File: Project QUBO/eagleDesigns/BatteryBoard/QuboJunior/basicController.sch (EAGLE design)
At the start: 11 parts, among them IC1 74AHCT1G08DBV, Q1 FDN5618P

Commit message: Final Design
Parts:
- added BATT, T_FUSE, WATER: (no value), pinhead:PINHD-1X2
- added C2, C6: 10nF, resistor:C-USC0805
- added C3, C5, C7: 100nF, resistor:C-USC0805
- added C4, C8: T491D475K050AT, resistor:CPOL-USCT7343
- added D1, D2: MMSD4148, diode:DIODE-SOD123
- added IC2: TLC2272D, texas:TLC2272D
- added IC3: 74LVC1G08DBV, 74xx-little-us:74LVC1G08DBV
- added LED1: Green, led:LEDCHIP-LED0805
- added R10, R4: 115k, resistor:R-US_R0805
- added R11, R6, R9: 1M, resistor:R-US_R0805
- added R12, R15, R17, R18: 100k, resistor:R-US_R0805
- added R13, R14, R5: 10k, resistor:R-US_R0805
- added R16: 470, resistor:R-US_R0805
- added R19: (no value), resistor:R-TRIMM3314J
- added R3: 845k, resistor:R-US_R0805
- added R7, R8: 3.3k, resistor:R-US_R0805
- added SK_DISABLE, SK_DISABLE1, TH_DISABLE: (no value), jumper:JP1E
- added U1, U2: LT3063, linear:LT3063
- IC1: value 74AHCT1G08DBV -> 74LVC1G08DBV; device 74xx-little-us:74AHCT1G08DBV -> 74xx-little-us:74LVC1G08DBV
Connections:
- removed net V+: Q1.D, R1.2
- new net BATT: BATT.1, Q1.D, R1.2
- new net N$10: IC2B.-IN, R12.2, R14.1
- new net N$11: IC2B.+IN, R17.1, R18.2
- new net N$12: R16.2, WATER.1
- new net N$13: R14.2, R15.2, R16.1
- new net N$14: IC2A.OUT, SK_DISABLE1.1
- new net N$15: IC2A.+IN, R19.S
- new net N$6: C2.1, U1.REF/BYP
- new net N$7: C6.1, U2.REF/BYP
- new net N$8: IC1A.I1, R11.2, TH_DISABLE.1, T_FUSE.2
- new net N$9: IC2A.-IN, IC2B.OUT, R12.1
- new net ON_SW: D1.C, ON.3, ON.4, ON_SW.1
- new net RELAY: C7.1, R9.2, U2.OUT
- new net SK: C5.1, IC3A.I0, R5.1, R6.2, SK_DISABLE.1
- new net SOFT_KILL: R5.2
- new net WATER: IC1A.I0, SK_DISABLE1.2
- net +5V: now also C3.1, IC2P.VCC, IC3P.VCC, R15.1, R17.2, R19.A, R3.2, SK_DISABLE.2, TH_DISABLE.2, T_FUSE.1, U1.OUT; no longer IC1P.VCC
- net FAULT: now also IC1A.O, IC3A.I1, OFF.3, OFF.4, OFF_SW.1; no longer IC1A.I0
- net FET: now also IC3A.O, R13.2; no longer IC1A.O
- net GND: now also BATT.2, C2.2, C3.2, C4.-, C5.2, C6.2, C7.2, C8.-, D2.A, IC2P.GND, IC3P.GND, LED1.C, ON.1, ON.2, ON_SW.2, R10.1, R11.1, R13.1, R18.1, R19.E, R4.1, R6.1, RELAY.2, U1.GND, U2.GND, WATER.2; no longer IC1P.GND
- net N$1: now also R10.2, R9.1, U2.ADJ; no longer ON.1, ON.2, ON_SW.2
- net N$2: now also R3.1, R4.2, U1.ADJ; no longer ON.3, ON.4, ON_SW.1
- net N$4: now also D1.A
- net N$5: now also LED1.A, R7.1, R8.1; no longer IC1A.I1, OFF.3, OFF.4, OFF_SW.1
- net VDD: now also C4.+, C8.+, D2.C, R7.2, R8.2, RELAY.1, U1.IN, U1.SHDN, U2.IN, U2.SHDN
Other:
- note added: "10V LDO"
- note added: "5V LDO"
- note added: "Connectors"
- note added: "Main Gate Control"
- note added: "Off Switch"
- note added: "On Indicator"
- note added: "On Switch"
- note added: "Power Switching"
- note added: "Secondary AND Gate"
- note added: "Water Sensor Amplifier"
- moved on the sheet: C1, IC1, N1, OFF, OFF_SW, ON, ON_SW, Q1, R1, R2, RELAY

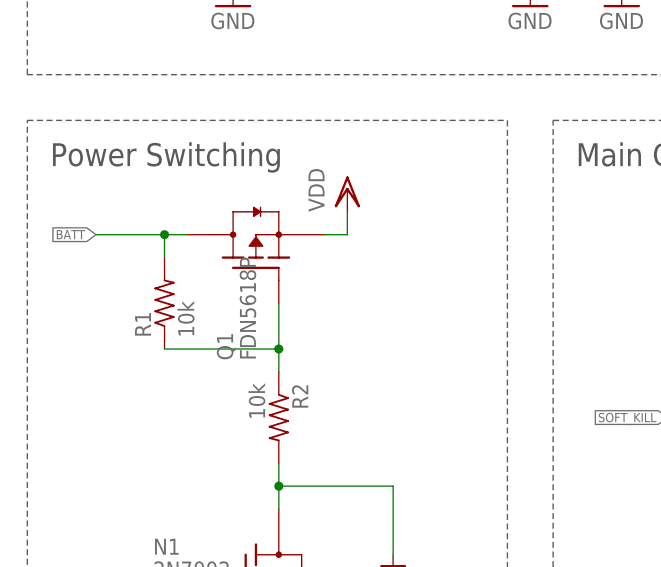
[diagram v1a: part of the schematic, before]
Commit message: 
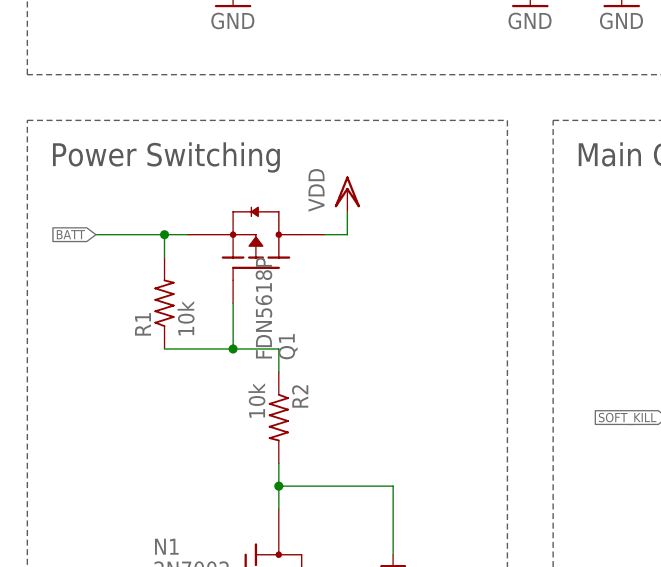
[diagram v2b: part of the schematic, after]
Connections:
- net BATT: now also Q1.S; no longer Q1.D
- net VDD: now also Q1.D; no longer Q1.S
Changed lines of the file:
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@@
 <?xml version="1.0" encoding="utf-8"?>
 <!DOCTYPE eagle SYSTEM "eagle.dtd">
-<eagle version="6.5.0">
+<eagle version="8.1.0">
 <drawing>
 <settings>
@@
 <grid distance="0.1" unitdist="inch" unit="inch" style="lines" multiple="1" display="no" altdistance="0.01" altunitdist="inch" altunit="inch"/>
 <layers>
-<layer number="1" name="Top" color="4" fill="1" visible="yes" active="no"/>
-<layer number="2" name="Route2" color="1" fill="3" visible="yes" active="no"/>
-<layer number="3" name="Route3" color="4" fill="3" visible="yes" active="no"/>
-<layer number="4" name="Route4" color="1" fill="4" visible="yes" active="no"/>
-<layer number="5" name="Route5" color="4" fill="4" visible="yes" active="no"/>
-<layer number="6" name="Route6" color="1" fill="8" visible="yes" active="no"/>
-<layer number="7" name="Route7" color="4" fill="8" visible="yes" active="no"/>
-<layer number="8" name="Route8" color="1" fill="2" visible="yes" active="no"/>
-<layer number="9" name="Route9" color="4" fill="2" visible="yes" active="no"/>
-<layer number="10" name="Route10" color="1" fill="7" visible="yes" active="no"/>
-<layer number="11" name="Route11" color="4" fill="7" visible="yes" active="no"/>
-<layer number="12" name="Route12" color="1" fill="5" visible="yes" active="no"/>
-<layer number="13" name="Route13" color="4" fill="5" visible="yes" active="no"/>
-<layer number="14" name="Route14" color="1" fill="6" visible="yes" active="no"/>
-<layer number="15" name="Route15" color="4" fill="6" visible="yes" active="no"/>
-<layer number="16" name="Bottom" color="1" fill="1" visible="yes" active="no"/>
-<layer number="17" name="Pads" color="2" fill="1" visible="yes" active="no"/>
-<layer number="18" name="Vias" color="2" fill="1" visible="yes" active="no"/>
-<layer number="19" name="Unrouted" color="6" fill="1" visible="yes" active="no"/>
-<layer number="20" name="Dimension" color="15" fill="1" visible="yes" active="no"/>
-<layer number="21" name="tPlace" color="7" fill="1" visible="yes" active="no"/>
-<layer number="22" name="bPlace" color="7" fill="1" visible="yes" active="no"/>
-<layer number="23" name="tOrigins" color="15" fill="1" visible="yes" active="no"/>
-<layer number="24" name="bOrigins" color="15" fill="1" visible="yes" active="no"/>
-<layer number="25" name="tNames" color="7" fill="1" visible="yes" active="no"/>
-<layer number="26" name="bNames" color="7" fill="1" visible="yes" active="no"/>
-<layer number="27" name="tValues" color="7" fill="1" visible="yes" active="no"/>
-<layer number="28" name="bValues" color="7" fill="1" visible="yes" active="no"/>
+<layer number="1" name="Top" color="4" fill="1" visible="no" active="no"/>
+<layer number="2" name="Route2" color="1" fill="3" visible="no" active="no"/>
+<layer number="3" name="Route3" color="4" fill="3" visible="no" active="no"/>
+<layer number="4" name="Route4" color="1" fill="4" visible="no" active="no"/>
+<layer number="5" name="Route5" color="4" fill="4" visible="no" active="no"/>
+<layer number="6" name="Route6" color="1" fill="8" visible="no" active="no"/>
+<layer number="7" name="Route7" color="4" fill="8" visible="no" active="no"/>
+<layer number="8" name="Route8" color="1" fill="2" visible="no" active="no"/>
+<layer number="9" name="Route9" color="4" fill="2" visible="no" active="no"/>
+<layer number="10" name="Route10" color="1" fill="7" visible="no" active="no"/>
+<layer number="11" name="Route11" color="4" fill="7" visible="no" active="no"/>
+<layer number="12" name="Route12" color="1" fill="5" visible="no" active="no"/>
+<layer number="13" name="Route13" color="4" fill="5" visible="no" active="no"/>
+<layer number="14" name="Route14" color="1" fill="6" visible="no" active="no"/>
+<layer number="15" name="Route15" color="4" fill="6" visible="no" active="no"/>
+<layer number="16" name="Bottom" color="1" fill="1" visible="no" active="no"/>
+<layer number="17" name="Pads" color="2" fill="1" visible="no" active="no"/>
+<layer number="18" name="Vias" color="2" fill="1" visible="no" active="no"/>
+<layer number="19" name="Unrouted" color="6" fill="1" visible="no" active="no"/>
+<layer number="20" name="Dimension" color="15" fill="1" visible="no" active="no"/>
+<layer number="21" name="tPlace" color="7" fill="1" visible="no" active="no"/>
+<layer number="22" name="bPlace" color="7" fill="1" visible="no" active="no"/>
+<layer number="23" name="tOrigins" color="15" fill="1" visible="no" active="no"/>
+<layer number="24" name="bOrigins" color="15" fill="1" visible="no" active="no"/>
+<layer number="25" name="tNames" color="7" fill="1" visible="no" active="no"/>
+<layer number="26" name="bNames" color="7" fill="1" visible="no" active="no"/>
+<layer number="27" name="tValues" color="7" fill="1" visible="no" active="no"/>
+<layer number="28" name="bValues" color="7" fill="1" visible="no" active="no"/>
 <layer number="29" name="tStop" color="7" fill="3" visible="no" active="no"/>
 <layer number="30" name="bStop" color="7" fill="6" visible="no" active="no"/>
@@
 <layer number="35" name="tGlue" color="7" fill="4" visible="no" active="no"/>
 <layer number="36" name="bGlue" color="7" fill="5" visible="no" active="no"/>
-<layer number="37" name="tTest" color="7" fill="1" visible="yes" active="no"/>
-<layer number="38" name="bTest" color="7" fill="1" visible="yes" active="no"/>
+<layer number="37" name="tTest" color="7" fill="1" visible="no" active="no"/>
+<layer number="38" name="bTest" color="7" fill="1" visible="no" active="no"/>
 <layer number="39" name="tKeepout" color="4" fill="11" visible="no" active="no"/>
 <layer number="40" name="bKeepout" color="1" fill="11" visible="no" active="no"/>
@@
 <layer number="44" name="Drills" color="7" fill="1" visible="no" active="no"/>
 <layer number="45" name="Holes" color="7" fill="1" visible="no" active="no"/>
-<layer number="46" name="Milling" color="3" fill="1" visible="yes" active="no"/>
-<layer number="47" name="Measures" color="7" fill="1" visible="yes" active="no"/>
-<layer number="48" name="Document" color="7" fill="1" visible="yes" active="no"/>
-<layer number="49" name="Reference" color="7" fill="1" visible="yes" active="no"/>
-<layer number="50" name="dxf" color="7" fill="1" visible="yes" active="no"/>
-<layer number="51" name="tDocu" color="7" fill="1" visible="yes" active="no"/>
-<layer number="52" name="bDocu" color="7" fill="1" visible="yes" active="no"/>
+<layer number="46" name="Milling" color="3" fill="1" visible="no" active="no"/>
+<layer number="47" name="Measures" color="7" fill="1" visible="no" active="no"/>
+<layer number="48" name="Document" color="7" fill="1" visible="no" active="no"/>
+<layer number="49" name="Reference" color="7" fill="1" visible="no" active="no"/>
+<layer number="50" name="dxf" color="7" fill="1" visible="no" active="no"/>
+<layer number="51" name="tDocu" color="7" fill="1" visible="no" active="no"/>
+<layer number="52" name="bDocu" color="7" fill="1" visible="no" active="no"/>
 <layer number="90" name="Modules" color="5" fill="1" visible="yes" active="yes"/>
 <layer number="91" name="Nets" color="2" fill="1" visible="yes" active="yes"/>
@@
 <instance part="OFF_SW" gate="G$1" x="27.94" y="182.88" rot="R270"/>
 <instance part="RELAY" gate="G$1" x="165.1" y="73.66"/>
-<instance part="Q1" gate="G$1" x="33.02" y="104.14" rot="R90"/>
+<instance part="Q1" gate="G$1" x="33.02" y="104.14" rot="MR90"/>
 <instance part="GND1" gate="1" x="12.7" y="187.96"/>
 <instance part="C1" gate="G$1" x="124.46" y="99.06"/>
@@
 <pinref part="VDD1" gate="G$1" pin="VDD"/>
 <wire x1="43.18" y1="109.22" x2="43.18" y2="106.68" width="0.1524" layer="91"/>
-<pinref part="Q1" gate="G$1" pin="S"/>
-<wire x1="43.18" y1="106.68" x2="40.64" y2="106.68" width="0.1524" layer="91"/>
+<pinref part="Q1" gate="G$1" pin="D"/>
+<wire x1="40.64" y1="106.68" x2="43.18" y2="106.68" width="0.1524" layer="91"/>
 </segment>
 <segment>
@@
 <net name="N$3" class="0">
 <segment>
-<pinref part="Q1" gate="G$1" pin="G"/>
 <pinref part="R2" gate="G$1" pin="1"/>
-<wire x1="35.56" y1="99.06" x2="35.56" y2="93.98" width="0.1524" layer="91"/>
 <pinref part="R1" gate="G$1" pin="1"/>
 <wire x1="35.56" y1="93.98" x2="35.56" y2="91.44" width="0.1524" layer="91"/>
-<wire x1="22.86" y1="93.98" x2="35.56" y2="93.98" width="0.1524" layer="91"/>
-<junction x="35.56" y="93.98"/>
+<wire x1="22.86" y1="93.98" x2="30.48" y2="93.98" width="0.1524" layer="91"/>
+<pinref part="Q1" gate="G$1" pin="G"/>
+<wire x1="30.48" y1="93.98" x2="35.56" y2="93.98" width="0.1524" layer="91"/>
+<wire x1="30.48" y1="99.06" x2="30.48" y2="93.98" width="0.1524" layer="91"/>
+<junction x="30.48" y="93.98"/>
 </segment>
 </net>
@@
 <net name="BATT" class="0">
 <segment>
-<pinref part="Q1" gate="G$1" pin="D"/>
-<wire x1="25.4" y1="106.68" x2="22.86" y2="106.68" width="0.1524" layer="91"/>
 <wire x1="22.86" y1="106.68" x2="15.24" y2="106.68" width="0.1524" layer="91"/>
 <pinref part="R1" gate="G$1" pin="2"/>
 <wire x1="22.86" y1="104.14" x2="22.86" y2="106.68" width="0.1524" layer="91"/>
+<label x="15.24" y="106.68" size="1.016" layer="95" rot="R180" xref="yes"/>
+<pinref part="Q1" gate="G$1" pin="S"/>
+<wire x1="22.86" y1="106.68" x2="25.4" y2="106.68" width="0.1524" layer="91"/>
 <junction x="22.86" y="106.68"/>
-<label x="15.24" y="106.68" size="1.016" layer="95" rot="R180" xref="yes"/>
-</segment>
-<segment>
+</segment>
+<segment>
